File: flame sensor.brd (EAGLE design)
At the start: 35 x 20 mm, 13 parts, among them T1 BPX81

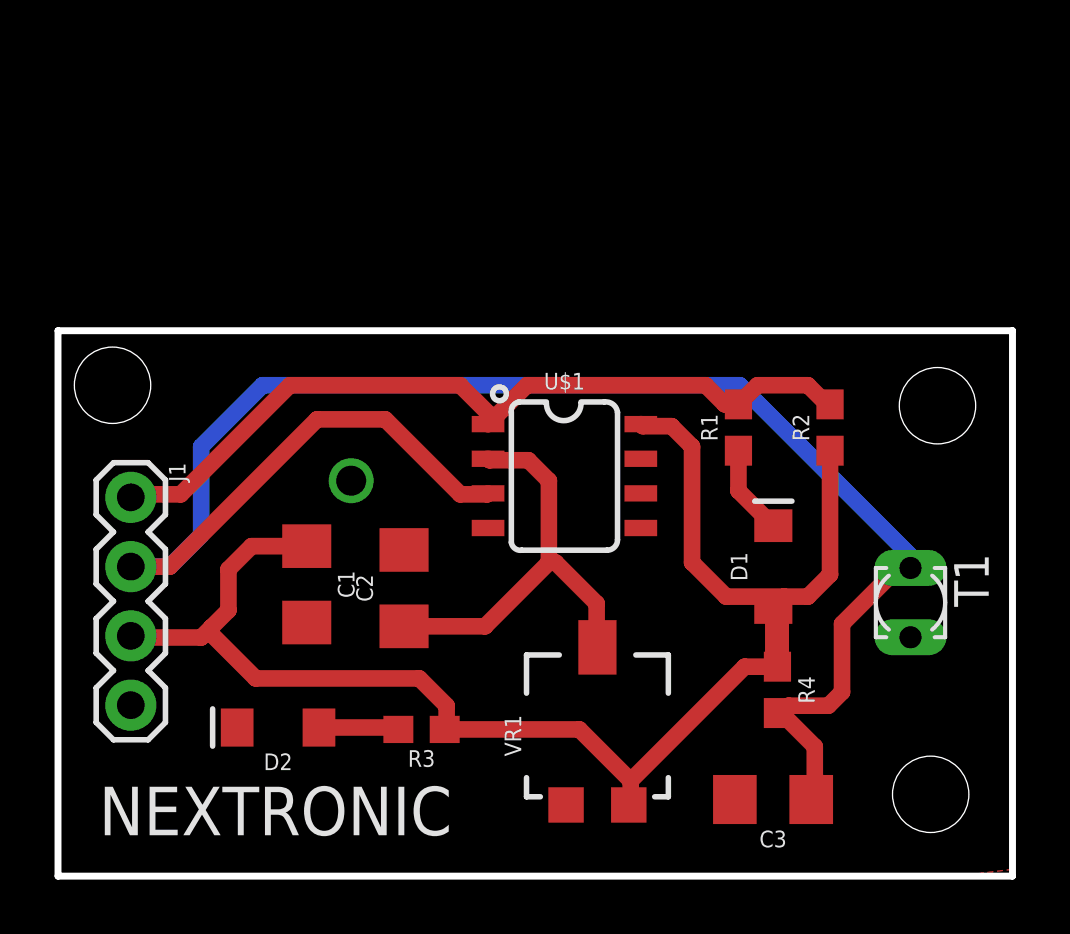
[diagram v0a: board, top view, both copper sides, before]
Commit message: changed capacitor
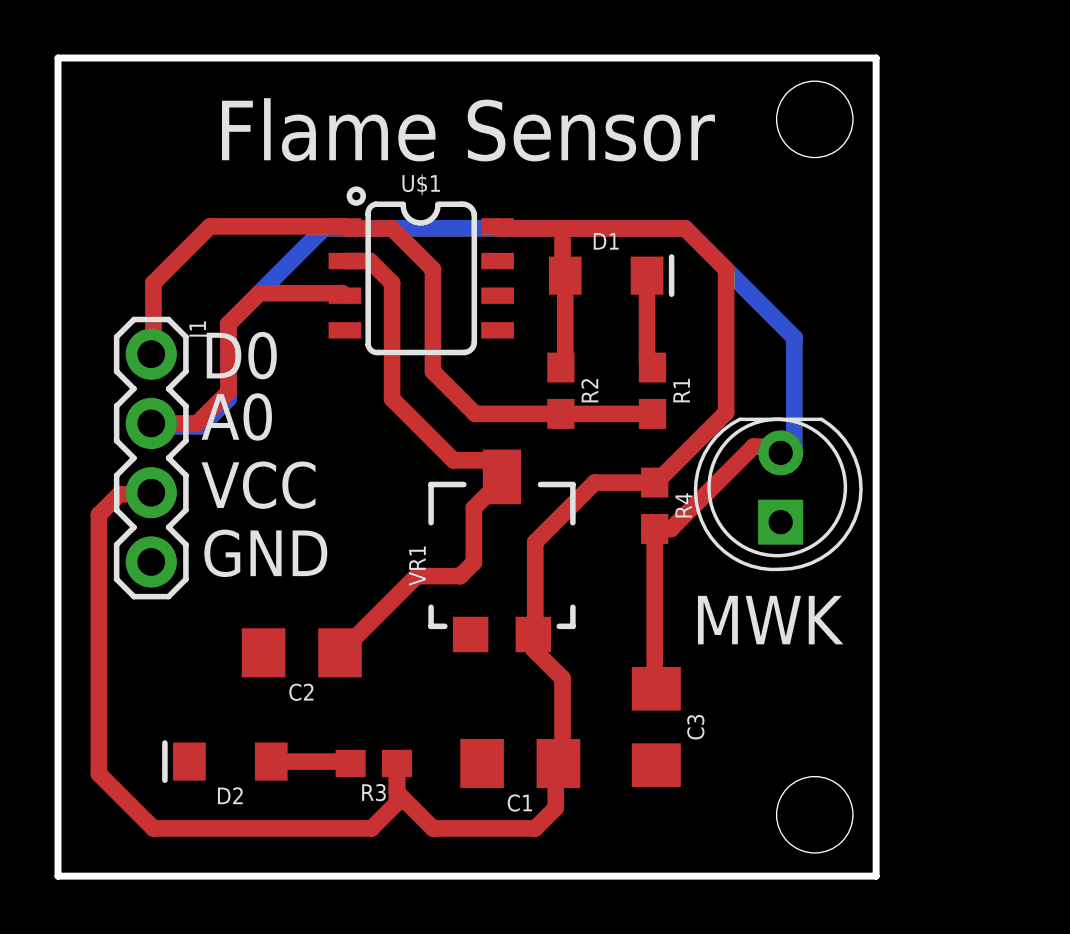
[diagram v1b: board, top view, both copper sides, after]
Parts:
- removed T1: BPX81, opto-trans-siemens:BPX81
- added U1: YG1006, template(1):2P-2.54-5MM
- moved D1 12.3 mm to (20.1, 22.0), turned to 0 degrees
- moved C1 10.2 mm to (16.9, 4.13), turned to 180 degrees
- moved R2 9.96 mm to (18.4, 17.8), turned to 270 degrees
- moved U$1 8.95 mm to (13.3, 21.9)
- moved R4 8.11 mm to (21.9, 13.6)
- moved VR1 7.16 mm to (16.3, 11.4)
- moved J1 5.30 mm to (3.42, 19.1)
- moved C3 5.04 mm to (21.9, 5.47), turned to 270 degrees
- moved C2 4.44 mm to (8.94, 8.19), turned to 180 degrees
- moved R1 3.43 mm to (21.8, 17.8), turned to 270 degrees
- moved D2 2.15 mm to (6.32, 4.20)
- moved R3 2.15 mm to (11.6, 4.13)
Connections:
- net A0: now also U1.2; no longer T1.E
- net GND: now also U1.1; no longer T1.C
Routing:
- net VCC: track 57.2 -> 71.9 mm
- net A0: track 65.1 -> 56.8 mm
- net N$2: track 15.8 -> 21.4 mm
- net D0: track 29.6 -> 26.8 mm
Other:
- board size 35 x 20 mm -> 30 x 30 mm
- board text added: "A0"
- board text added: "D0"
- board text added: "Flame Sensor"
- board text added: "GND"
- board text added: "MWK"
- board text added: "VCC"
- board text removed: "NEXTRONIC"
